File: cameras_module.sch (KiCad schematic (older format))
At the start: 30 parts, among them J2 WE_68715014522, U5 NTS0102GT, U6 PCA9547BS

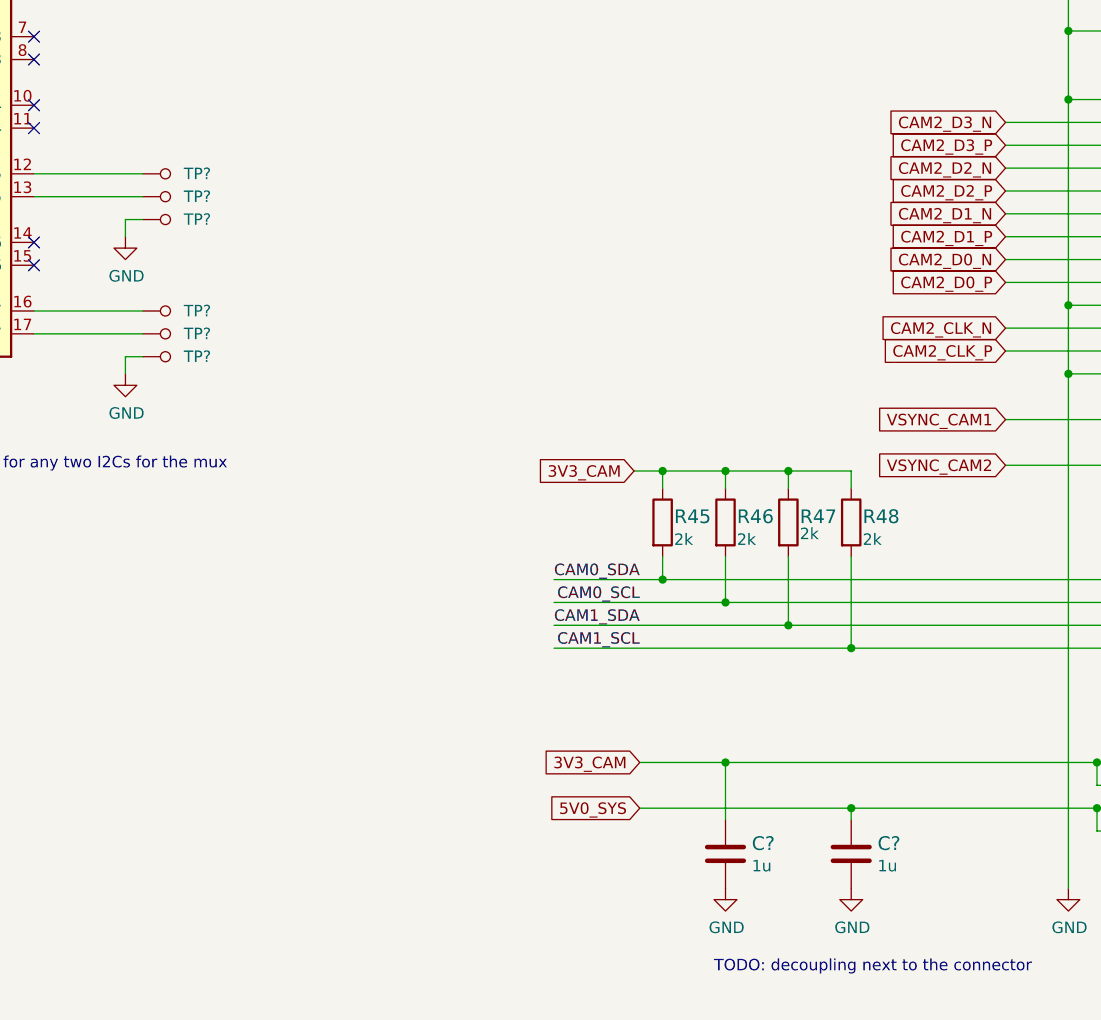
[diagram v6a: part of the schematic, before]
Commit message: Corrected power supplies. Change of TP to 1,5mm
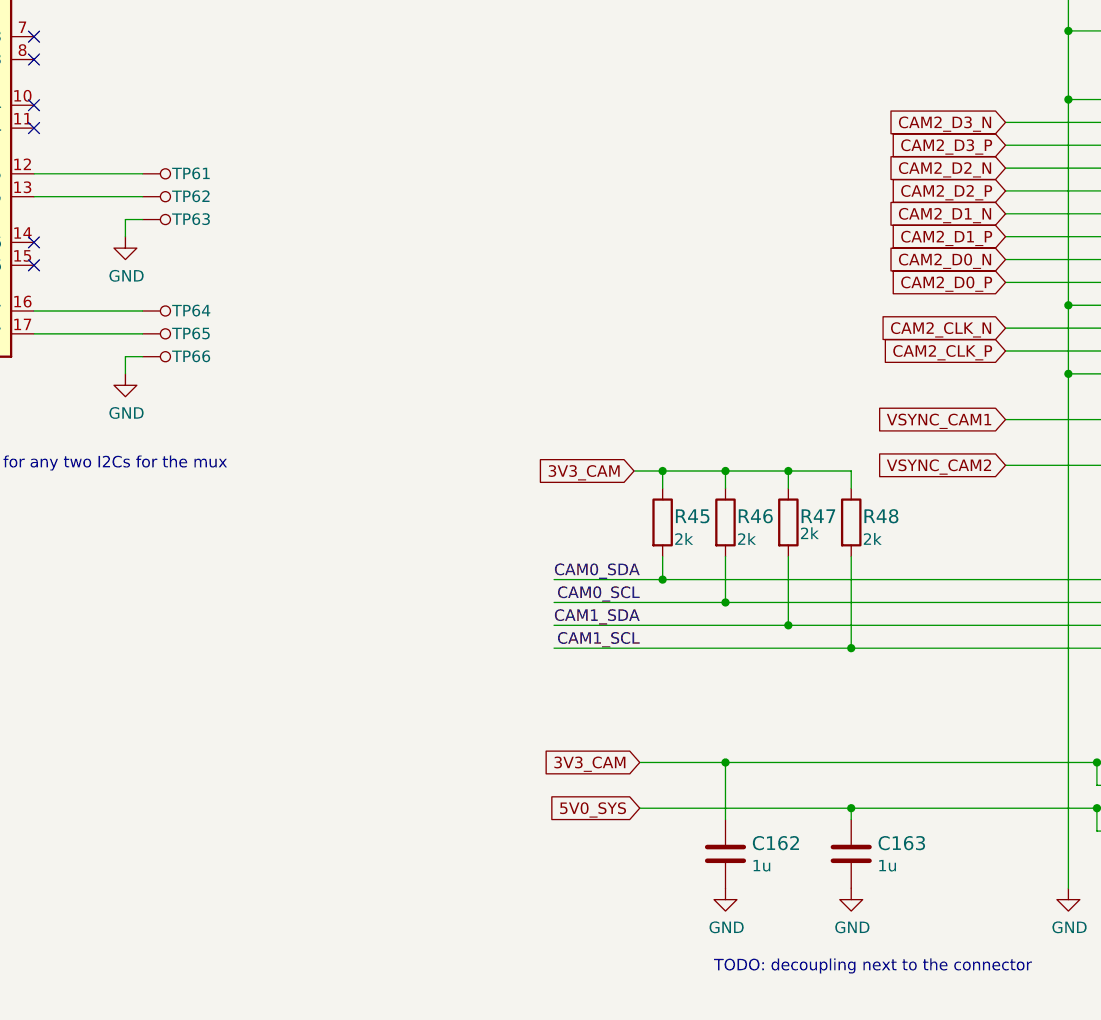
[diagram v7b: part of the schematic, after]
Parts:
- TP61, TP62, TP63, TP64, TP65, TP66: renamed from TP?; value TP_SMD_0_75MM -> TP_SMD_1_5MM; footprint sc606-baseboard-footprints:Testpoint_smd_0_75mm -> sc606-baseboard-footprints:TP-R-1.5
- U6: footprint antmicro-footprints:HVQFN24 -> sc606-baseboard-footprints:HVQFN24
- gave numbers to parts that had none: 2
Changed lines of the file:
@@
 	6800 2525 7100 2525
 $Comp
-L sc606-baseboard:GND #PWR?
+L sc606-baseboard:GND #PWR0225
 U 1 1 63CDCAEA
 P 6500 2875
-F 0 "#PWR?" H 6500 2625 50  0001 C CNN
+F 0 "#PWR0225" H 6500 2625 50  0001 C CNN
 F 1 "GND" H 6505 2702 50  0000 C CNN
 F 2 "" H 6500 2875 50  0001 C CNN
@@
 F 0 "U6" H 8375 5514 60  0000 C CNN
 F 1 "PCA9547BS" H 8375 5408 60  0000 C CNN
-F 2 "antmicro-footprints:HVQFN24" H 8225 2725 60  0001 C CNN
+F 2 "sc606-baseboard-footprints:HVQFN24" H 8225 2725 60  0001 C CNN
 F 3 "https://www.nxp.com/docs/en/data-sheet/PCA9547.pdf" H 8475 4125 60  0001 C CNN
 F 4 " NXP" H 8475 4125 50  0001 C CNN "Manufacturer"
@@
 	7850 3925 7850 4025
 $Comp
-L sc606-baseboard:GND #PWR?
+L sc606-baseboard:GND #PWR0226
 U 1 1 63D3BEB8
 P 7850 4025
-F 0 "#PWR?" H 7850 3775 50  0001 C CNN
+F 0 "#PWR0226" H 7850 3775 50  0001 C CNN
 F 1 "GND" H 7855 3852 50  0000 C CNN
 F 2 "" H 7850 4025 50  0001 C CNN
@@
 P 9350 4525
 AR Path="/61D43102/63FF239B" Ref="TP?"  Part="1"
-AR Path="/61D49F95/63FF239B" Ref="TP?"  Part="1"
-F 0 "TP?" V 9350 4325 50  0000 L CNN
-F 1 "TP_SMD_0_75MM" H 9350 4425 50  0001 C CNN
-F 2 "sc606-baseboard-footprints:Testpoint_smd_0_75mm" H 9550 4725 60  0001 L CNN
+AR Path="/61D49F95/63FF239B" Ref="TP61"  Part="1"
+F 0 "TP61" V 9350 4325 50  0000 L CNN
+F 1 "TP_SMD_1_5MM" H 9350 4425 50  0001 C CNN
+F 2 "sc606-baseboard-footprints:TP-R-1.5" H 9550 4725 60  0001 L CNN
 F 3 "" H 9550 4825 60  0001 L CNN
 	1    9350 4525
@@
 P 9350 4625
 AR Path="/61D43102/63FF23A1" Ref="TP?"  Part="1"
-AR Path="/61D49F95/63FF23A1" Ref="TP?"  Part="1"
-F 0 "TP?" V 9350 4425 50  0000 L CNN
-F 1 "TP_SMD_0_75MM" H 9350 4525 50  0001 C CNN
-F 2 "sc606-baseboard-footprints:Testpoint_smd_0_75mm" H 9550 4825 60  0001 L CNN
+AR Path="/61D49F95/63FF23A1" Ref="TP62"  Part="1"
+F 0 "TP62" V 9350 4425 50  0000 L CNN
+F 1 "TP_SMD_1_5MM" H 9350 4525 50  0001 C CNN
+F 2 "sc606-baseboard-footprints:TP-R-1.5" H 9550 4825 60  0001 L CNN
 F 3 "" H 9550 4925 60  0001 L CNN
 	1    9350 4625
@@
 P 9350 4725
 AR Path="/61D43102/6400A3CB" Ref="TP?"  Part="1"
-AR Path="/61D49F95/6400A3CB" Ref="TP?"  Part="1"
-F 0 "TP?" V 9350 4525 50  0000 L CNN
-F 1 "TP_SMD_0_75MM" H 9350 4625 50  0001 C CNN
-F 2 "sc606-baseboard-footprints:Testpoint_smd_0_75mm" H 9550 4925 60  0001 L CNN
+AR Path="/61D49F95/6400A3CB" Ref="TP63"  Part="1"
+F 0 "TP63" V 9350 4525 50  0000 L CNN
+F 1 "TP_SMD_1_5MM" H 9350 4625 50  0001 C CNN
+F 2 "sc606-baseboard-footprints:TP-R-1.5" H 9550 4925 60  0001 L CNN
 F 3 "" H 9550 5025 60  0001 L CNN
 	1    9350 4725
@@
 	9175 4725 9175 4800
 $Comp
-L sc606-baseboard:GND #PWR?
+L sc606-baseboard:GND #PWR0227
 U 1 1 64010BB2
 P 9175 4800
-F 0 "#PWR?" H 9175 4550 50  0001 C CNN
+F 0 "#PWR0227" H 9175 4550 50  0001 C CNN
 F 1 "GND" H 9180 4627 50  0000 C CNN
 F 2 "" H 9175 4800 50  0001 C CNN
@@
 P 9350 5125
 AR Path="/61D43102/640131A9" Ref="TP?"  Part="1"
-AR Path="/61D49F95/640131A9" Ref="TP?"  Part="1"
-F 0 "TP?" V 9350 4925 50  0000 L CNN
-F 1 "TP_SMD_0_75MM" H 9350 5025 50  0001 C CNN
-F 2 "sc606-baseboard-footprints:Testpoint_smd_0_75mm" H 9550 5325 60  0001 L CNN
+AR Path="/61D49F95/640131A9" Ref="TP64"  Part="1"
+F 0 "TP64" V 9350 4925 50  0000 L CNN
+F 1 "TP_SMD_1_5MM" H 9350 5025 50  0001 C CNN
+F 2 "sc606-baseboard-footprints:TP-R-1.5" H 9550 5325 60  0001 L CNN
 F 3 "" H 9550 5425 60  0001 L CNN
 	1    9350 5125
@@
 P 9350 5225
 AR Path="/61D43102/640131AF" Ref="TP?"  Part="1"
-AR Path="/61D49F95/640131AF" Ref="TP?"  Part="1"
-F 0 "TP?" V 9350 5025 50  0000 L CNN
-F 1 "TP_SMD_0_75MM" H 9350 5125 50  0001 C CNN
-F 2 "sc606-baseboard-footprints:Testpoint_smd_0_75mm" H 9550 5425 60  0001 L CNN
+AR Path="/61D49F95/640131AF" Ref="TP65"  Part="1"
+F 0 "TP65" V 9350 5025 50  0000 L CNN
+F 1 "TP_SMD_1_5MM" H 9350 5125 50  0001 C CNN
+F 2 "sc606-baseboard-footprints:TP-R-1.5" H 9550 5425 60  0001 L CNN
 F 3 "" H 9550 5525 60  0001 L CNN
 	1    9350 5225
@@
 P 9350 5325
 AR Path="/61D43102/640131B7" Ref="TP?"  Part="1"
-AR Path="/61D49F95/640131B7" Ref="TP?"  Part="1"
-F 0 "TP?" V 9350 5125 50  0000 L CNN
-F 1 "TP_SMD_0_75MM" H 9350 5225 50  0001 C CNN
-F 2 "sc606-baseboard-footprints:Testpoint_smd_0_75mm" H 9550 5525 60  0001 L CNN
+AR Path="/61D49F95/640131B7" Ref="TP66"  Part="1"
+F 0 "TP66" V 9350 5125 50  0000 L CNN
+F 1 "TP_SMD_1_5MM" H 9350 5225 50  0001 C CNN
+F 2 "sc606-baseboard-footprints:TP-R-1.5" H 9550 5525 60  0001 L CNN
 F 3 "" H 9550 5625 60  0001 L CNN
 	1    9350 5325
@@
 	9175 5325 9175 5400
 $Comp
-L sc606-baseboard:GND #PWR?
+L sc606-baseboard:GND #PWR0228
 U 1 1 640131BF
 P 9175 5400
-F 0 "#PWR?" H 9175 5150 50  0001 C CNN
+F 0 "#PWR0228" H 9175 5150 50  0001 C CNN
 F 1 "GND" H 9180 5227 50  0000 C CNN
 F 2 "" H 9175 5400 50  0001 C CNN
@@
 P 12350 7500
 AR Path="/61D43102/6404EB69" Ref="C?"  Part="1"
-AR Path="/61D49F95/6404EB69" Ref="C?"  Part="1"
-F 0 "C?" H 12465 7545 60  0000 L CNN
+AR Path="/61D49F95/6404EB69" Ref="C163"  Part="1"
+F 0 "C163" H 12465 7545 60  0000 L CNN
 F 1 "C_1u_0402" H 12350 7350 60  0001 C CNN
 F 2 "sc606-baseboard-footprints:0402-cap" H 12550 7700 60  0001 L CNN
@@
 P 11800 7500
 AR Path="/61D43102/64084FB5" Ref="C?"  Part="1"
-AR Path="/61D49F95/64084FB5" Ref="C?"  Part="1"
-F 0 "C?" H 11915 7545 60  0000 L CNN
+AR Path="/61D49F95/64084FB5" Ref="C162"  Part="1"
+F 0 "C162" H 11915 7545 60  0000 L CNN
 F 1 "C_1u_0402" H 11800 7350 60  0001 C CNN
 F 2 "sc606-baseboard-footprints:0402-cap" H 12000 7700 60  0001 L CNN
@@
 $EndComp
 $Comp
-L sc606-baseboard:GND #PWR?
+L sc606-baseboard:GND #PWR0229
 U 1 1 6408E41B
 P 11800 7650
-F 0 "#PWR?" H 11800 7400 50  0001 C CNN
+F 0 "#PWR0229" H 11800 7400 50  0001 C CNN
 F 1 "GND" H 11805 7477 50  0000 C CNN
 F 2 "" H 11800 7650 50  0001 C CNN
@@
 $EndComp
 $Comp
-L sc606-baseboard:GND #PWR?
+L sc606-baseboard:GND #PWR0230
 U 1 1 6408E75F
 P 12350 7650
-F 0 "#PWR?" H 12350 7400 50  0001 C CNN
+F 0 "#PWR0230" H 12350 7400 50  0001 C CNN
 F 1 "GND" H 12355 7477 50  0000 C CNN
 F 2 "" H 12350 7650 50  0001 C CNN
